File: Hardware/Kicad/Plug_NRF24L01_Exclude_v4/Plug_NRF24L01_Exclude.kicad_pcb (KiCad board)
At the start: 2 copper layers, 36 x 24 mm, 39 parts, among them J1 Conn_02x07_Odd_Even, J2 Conn_01x08_Socket, J3 Conn_01x07_Socket, Q1 2N7002, Q2 2N7002, Q3 2N7002, Q4 2N7002, Q5 2N7002, SW1 SW_SPST, U1 STM32L412KBTx, U2 MIC5219-3.3YMM

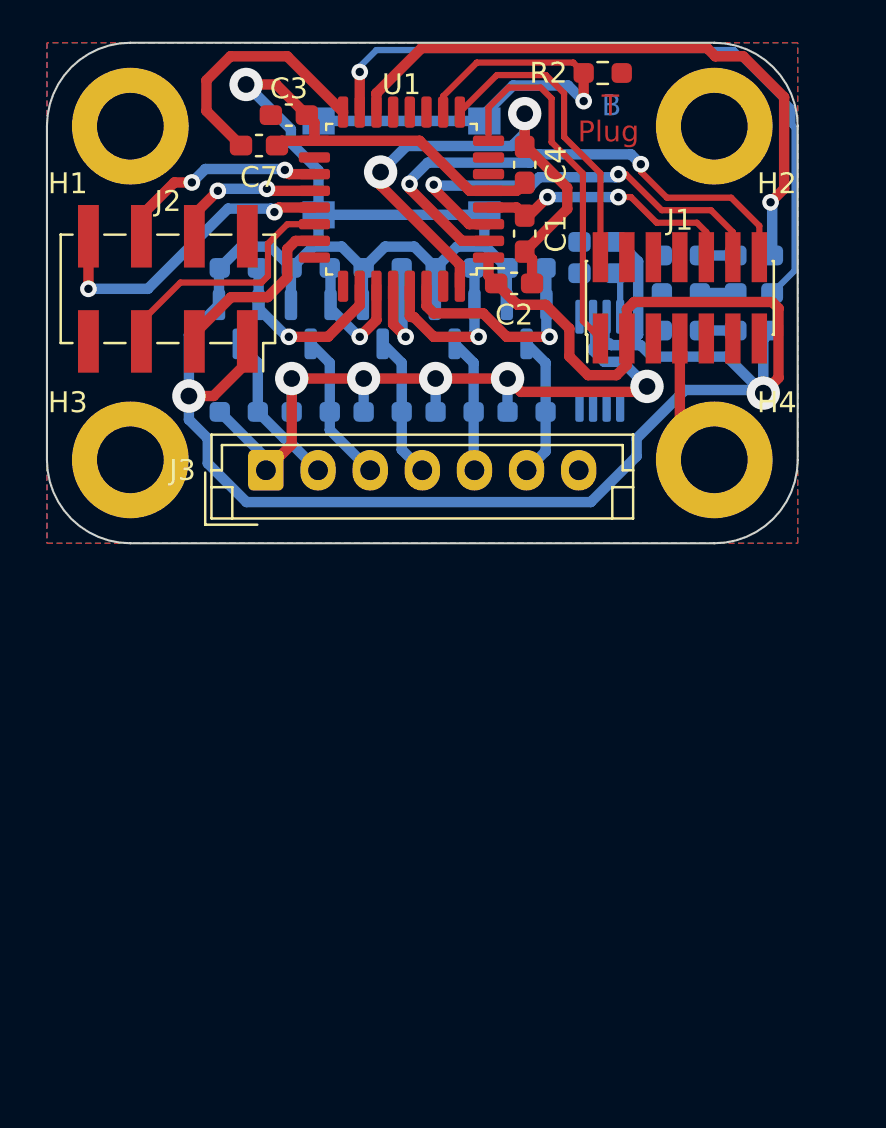
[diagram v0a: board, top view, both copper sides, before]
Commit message: Update Plug_NRF24L01_Exclude v4.0a (Schematic Fixes / New PCB Routing) - Added new images
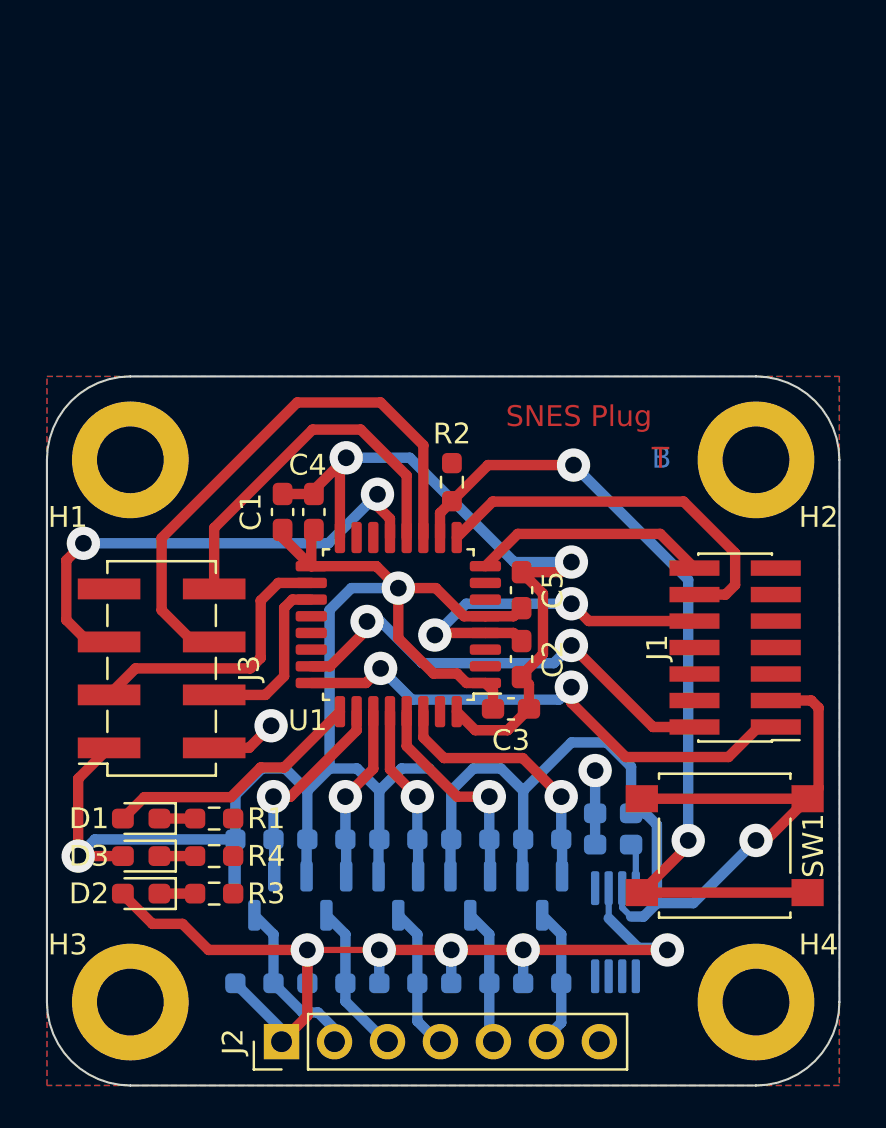
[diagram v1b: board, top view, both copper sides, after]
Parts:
- D1, D2, D3, R1, R3, R4, SW1: moved to F.Cu
- J2: renamed from J3; footprint Connector_JST:JST_EH_B7B-EH-A_1x07_P2.50mm_Vertical -> Connector_PinHeader_2.54mm:PinHeader_1x07_P2.54mm_Vertical
- moved D2 41.1 mm to (100.5, 120.8), turned to 180 degrees
- moved D1 39.9 mm to (100.5, 117.2), turned to 180 degrees
- moved D3 38.7 mm to (100.5, 119.0), turned to 180 degrees
- moved R3 36.5 mm to (104.0, 120.8), turned to 0 degrees
- moved SW1 36.0 mm to (128.5, 118.5)
- moved R1 35.1 mm to (104.0, 117.2), turned to 0 degrees
- moved R4 33.7 mm to (104.0, 119.0), turned to 0 degrees
- moved C6 27.4 mm to (123.2, 118.5)
- moved C7 27.4 mm to (123.2, 117.0)
- moved J2 27.4 mm to (107.2, 127.9), turned to 90 degrees
- moved Q1 27.4 mm to (106.0, 120.9)
- moved Q2 27.4 mm to (109.4, 120.9)
- moved Q3 27.4 mm to (112.8, 120.9)
- moved Q4 27.4 mm to (116.3, 120.9)
- moved Q5 27.4 mm to (119.8, 120.9)
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- renumbered C7 to C1, C1 to C2, C2 to C3, C3 to C4, C4 to C5, C5 to C6, C6 to C7, J2 to J3
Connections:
- D1 pad 2: Player1_LED -> Status_LED
- D2 pad 2: Status_LED -> +5V
- U1 pad 11: unconnected-(U1-PA5-Pad11) -> SPI_Clock
- U1 pad 12: unconnected-(U1-PA6-Pad12) -> SPI_Digital_Input
- U1 pad 13: unconnected-(U1-PA7-Pad13) -> SPI_Digital_Output
- U1 pad 14: Player1_LED -> unconnected-(U1-PB0-Pad14)
- U1 pad 15: Status_LED -> unconnected-(U1-PB1-Pad15)
- U1 pad 18: unconnected-(U1-PA8-Pad18) -> SPI_Chip_Select
- U1 pad 19: SPI_Clock -> Chip_Enable
- U1 pad 2: USART2_TX -> unconnected-(U1-PC14-Pad2)
- U1 pad 20: Chip_Enable -> unconnected-(U1-PA10-Pad20)
- U1 pad 21: SPI_Digital_Input -> unconnected-(U1-PA11-Pad21)
- U1 pad 22: SPI_Digital_Output -> unconnected-(U1-PA12-Pad22)
- U1 pad 23: SPI_Chip_Select -> SWDIO
- U1 pad 24: unconnected-(U1-PA14-Pad24) -> SWDCK
- U1 pad 25: unconnected-(U1-PA15-Pad25) -> Status_LED
- U1 pad 3: USART2_RX -> unconnected-(U1-PC15-Pad3)
- U1 pad 8: SWDCK -> USART2_TX
- U1 pad 9: SWDIO -> USART2_RX
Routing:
- net Player1_LED: track 30.2 -> 0.00 mm, vias 1 -> 0
- net Status_LED: track 33.8 -> 12.5 mm, vias 1 -> 0
- net +3.3V: track 149.8 -> 130.3 mm
- net SPI_Clock: track 10.3 -> 27.1 mm, vias 2 -> 0
- net Appairing_Btn: track 23.6 -> 40.2 mm, vias 1 -> 2
- net USART2_TX: track 25.6 -> 11.3 mm, vias 2 -> 0
- net SPI_Digital_Output: track 12.1 -> 23.9 mm, vias 0 -> 2
- net +5V: track 37.4 -> 47.2 mm
- net SWDCK: track 17.7 -> 25.9 mm, vias 0 -> 2
- net SWDIO: track 14.7 -> 22.3 mm, vias 0 -> 2
- net NRST: track 12.9 -> 17.8 mm
- net SPI_Chip_Select: track 8.76 -> 13.5 mm
- net SPI_Digital_Input: track 15.1 -> 18.0 mm, vias 2 -> 0
- net Serial_Data1_STM32: track 6.05 -> 8.45 mm
- net GND: track 44.1 -> 41.9 mm, vias 2 -> 4
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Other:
- board size 36 x 24 mm -> 38 x 34 mm
- board text added: "SNES Plug"
- board text removed: "Plug"
